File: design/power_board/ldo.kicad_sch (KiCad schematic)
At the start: 9 parts, among them U2 LM317M_DCY_4

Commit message: Add files via upload
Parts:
- removed C?: 10uF 35V, Capacitor_SMD:C_0805_2012Metric_Pad1.18x1.45mm_HandSolder, symbol Device:C
- removed C?: OPT, Capacitor_SMD:C_0805_2012Metric_Pad1.18x1.45mm_HandSolder, symbol Device:C
- added C?: 10uF, Capacitor_SMD:C_0805_2012Metric_Pad1.18x1.45mm_HandSolder, symbol Device:C
- C? (x2): value 10uF 35V -> 10uF
- R? (x2): value 442k -> _k
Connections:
- net GND: now also C?.1
- net at D?.2 (A), R?.2: now also R?.1, U2.4 (ADJUST), C?.2; no longer D?.1 (K), U2.1 (OUTPUT)
- new net: D?.1 (K), R?.1, U2.1 (OUTPUT)
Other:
- note added: "200mA output current"
- note added: "R2 = R1(VOUT/1.25 - 1)"
- note added: "Resistor values for R8 = 10k: R9 sets the voltage output for 20V R9 = 10(20/1.25 - 1) R9 = 170k for 12V: R9 = 10(12/1.25 - 1) R9 = 86k for 10V: R9 = 10(10/1.25 - 1) R9 = 70k for 5V: R9 = 10(5/1.25 - 1) R9 = 30k Both 1%"
- note removed: "A resistor between SET and GND sets the output voltage based on a 200uA current source (two LDOs). R(kΩ) = 5*VOUT"
- note removed: "The 20mR resistors somehow make the LDOs share the current, idk check the datasheet."
- note removed: "When PGFB is below 300mV fast startup is enabled. SETFS is a resistor to ground which should divide VOUT such that PGFB reaches 300mV at 90% of the desired VOUT. (pg. 21) R(kΩ) = 442 / (3*VOUT - 1)"
- moved on the sheet: R?

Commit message: Add files via upload
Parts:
- added C?: 0.1uF, Capacitor_SMD:C_0805_2012Metric_Pad1.18x1.45mm_HandSolder, symbol Device:C
- R?: value _k -> 10k
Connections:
- net GND: now also C?.2
- net VIN: now also C?.1
- net VOUT: now also U2.1 (OUTPUT); no longer D?.2 (A), U2.3 (OUTPUT)
- net at C?.2, D?.2 (A), R?.1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: now also R?.1; no longer R?.2
- new net: D?.1 (K), D?.2 (A), R?.2, U2.3 (OUTPUT)
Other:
- moved on the sheet: C?, D?, R?, U2

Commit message: Changed footprint Changed footprint path changed footprint Edit Edit Edit
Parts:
- U2: footprint footprints:DCY4 -> Package_TO_SOT_SMD:SOT-223-3_TabPin2
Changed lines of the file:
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@@
       (effects (font (size 1.524 1.524)))
     )
-    (property "Footprint" "footprints:DCY4" (at 137.16 80.01 0)
+    (property "Footprint" "Package_TO_SOT_SMD:SOT-223-3_TabPin2" (at 137.16 80.01 0)
       (effects (font (size 1.524 1.524)) hide)
     )

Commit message: Edited calculations
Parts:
- R?: value 10k -> 0.24k
- U2: value LM317M_DCY_4 -> LM317M_DCY
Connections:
- net VOUT: now also D?.1 (K), D?.2 (A), R?.2, U2.3 (OUTPUT); no longer U2.1 (OUTPUT)
- net at C?.2, D?.2 (A), R?.1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: no longer R?.1
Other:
- note added: "Resistor values for R8 = 0.24k: R9 sets the voltage output for 20V R9 = 0.24(20/1.25 - 1) R9 = 3.6k for 12V: R9 = 0.24(12/1.25 - 1) R9 = 2.06k for 10V: R9 = 0.24(10/1.25 - 1) R9 = 1.68k for 5V: R9 = 0.24(5/1.25 - 1) R9 = 0.72k Both 1%"
- note removed: "Resistor values for R8 = 10k: R9 sets the voltage output for 20V R9 = 10(20/1.25 - 1) R9 = 170k for 12V: R9 = 10(12/1.25 - 1) R9 = 86k for 10V: R9 = 10(10/1.25 - 1) R9 = 70k for 5V: R9 = 10(5/1.25 - 1) R9 = 30k Both 1%"
- moved on the sheet: C?, R?
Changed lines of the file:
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@@
 (kicad_sch (version 20230121) (generator eeschema)
   (paper "A4")
+  (junction (at 198.12 95.25) (diameter 0) (color 0 0 0 0)
+  )
   (junction (at 163.83 95.25) (diameter 0) (color 0 0 0 0)
   )
   (junction (at 201.93 78.74) (diameter 0) (color 0 0 0 0)
   )
+  (junction (at 163.83 114.3) (diameter 0) (color 0 0 0 0)
+  )
   (junction (at 179.07 114.3) (diameter 0) (color 0 0 0 0)
   )
   (junction (at 170.18 95.25) (diameter 0) (color 0 0 0 0)
   )
-  (junction (at 106.68 95.25) (diameter 0) (color 0 0 0 0)
-  )
-  (junction (at 163.83 114.3) (diameter 0) (color 0 0 0 0)
-  )
   (junction (at 189.23 78.74) (diameter 0) (color 0 0 0 0)
   )
+  (junction (at 179.07 95.25) (diameter 0) (color 0 0 0 0)
+  )
   (junction (at 170.18 78.74) (diameter 0) (color 0 0 0 0)
   )
-  (wire (pts (xy 163.83 114.3) (xy 163.83 118.11))
+  (wire (pts (xy 157.48 114.3) (xy 157.48 118.11))
     (stroke (width 0) (type default))
   )
@@
     (stroke (width 0) (type default))
   )
+  (wire (pts (xy 198.12 95.25) (xy 210.82 95.25))
+    (stroke (width 0) (type default))
+  )
   (wire (pts (xy 170.18 95.25) (xy 163.83 95.25))
     (stroke (width 0) (type default))
   )
+  (wire (pts (xy 158.75 114.3) (xy 163.83 114.3))
+    (stroke (width 0) (type default))
+  )
   (wire (pts (xy 170.18 78.74) (xy 189.23 78.74))
     (stroke (width 0) (type default))
@@
     (stroke (width 0) (type default))
   )
-  (wire (pts (xy 114.3 95.25) (xy 106.68 95.25))
-    (stroke (width 0) (type default))
-  )
   (wire (pts (xy 189.23 78.74) (xy 201.93 78.74))
     (stroke (width 0) (type default))
@@
     (stroke (width 0) (type default))
   )
-  (wire (pts (xy 106.68 95.25) (xy 90.17 95.25))
+  (wire (pts (xy 198.12 95.25) (xy 179.07 95.25))
     (stroke (width 0) (type default))
   )
@@
     (stroke (width 0) (type default))
   )
-  (wire (pts (xy 158.75 114.3) (xy 163.83 114.3))
-    (stroke (width 0) (type default))
-  )
-  (text "R2 = R1(VOUT/1.25 - 1)" (at 132.08 124.46 0)
+  (text "R2 = R1(VOUT/1.25 - 1)" (at 127 123.19 0)
     (effects (font (size 1.27 1.27)) (justify left bottom))
   )
@@
     (effects (font (size 1.27 1.27)) (justify right bottom))
   )
-  (text "Resistor values for R8 = 10k:\nR9\n sets the voltage output\nfor 20V \n	R9 = 10(20/1.25 - 1)\n	R9 = 170k\n\nfor 12V:\n  R9 = 10(12/1.25 - 1)\n  R9 = 86k\n\nfor 10V:\n  R9 = 10(10/1.25 - 1)\n  R9 = 70k\n\nfor 5V:\n  R9 = 10(5/1.25 - 1)\n  R9 = 30k\n\nBoth 1%"
-    (at 186.69 146.05 0)
+  (text "Resistor values for R8 = 0.24k:\nR9\n sets the voltage output\nfor 20V \n	R9 = 0.24(20/1.25 - 1)\n	R9 = 3.6k\n\nfor 12V:\n  R9 = 0.24(12/1.25 - 1)\n  R9 = 2.06k\n\nfor 10V:\n  R9 = 0.24(10/1.25 - 1)\n  R9 = 1.68k\n\nfor 5V:\n  R9 = 0.24(5/1.25 - 1)\n  R9 = 0.72k\n\nBoth 1%"
+    (at 242.57 134.62 0)
     (effects (font (size 1.27 1.27)) (justify left bottom))
   )
@@
     (effects (font (size 1.27 1.27)) (justify left))
   )
-  (hierarchical_label "VOUT" (shape output) (at 90.17 95.25 180) (fields_autoplaced)
-    (effects (font (size 1.27 1.27)) (justify right))
-  )
-  (symbol (lib_id "power:GND") (at 106.68 102.87 0) (mirror y) (unit 1)
-    (in_bom yes) (on_board yes) (dnp no)
-    (property "Reference" "#PWR?" (at 106.68 109.22 0)
-      (effects (font (size 1.27 1.27)) hide)
-    )
-    (property "Value" "GND" (at 106.553 107.2642 0)
-      (effects (font (size 1.27 1.27)))
-    )
-    (property "Footprint" "" (at 106.68 102.87 0)
-      (effects (font (size 1.27 1.27)) hide)
-    )
-    (property "Datasheet" "" (at 106.68 102.87 0)
+  (hierarchical_label "VOUT" (shape output) (at 210.82 95.25 0) (fields_autoplaced)
+    (effects (font (size 1.27 1.27)) (justify left))
+  )
+  (symbol (lib_id "power:GND") (at 198.12 102.87 0) (mirror y) (unit 1)
+    (in_bom yes) (on_board yes) (dnp no)
+    (property "Reference" "#PWR?" (at 198.12 109.22 0)
+      (effects (font (size 1.27 1.27)) hide)
+    )
+    (property "Value" "GND" (at 197.993 107.2642 0)
+      (effects (font (size 1.27 1.27)))
+    )
+    (property "Footprint" "" (at 198.12 102.87 0)
+      (effects (font (size 1.27 1.27)) hide)
+    )
+    (property "Datasheet" "" (at 198.12 102.87 0)
       (effects (font (size 1.27 1.27)) hide)
     )
@@
     )
   )
-  (symbol (lib_id "power:GND") (at 163.83 125.73 0) (unit 1)
-    (in_bom yes) (on_board yes) (dnp no)
-    (property "Reference" "#PWR?" (at 163.83 132.08 0)
-      (effects (font (size 1.27 1.27)) hide)
-    )
-    (property "Value" "GND" (at 163.957 130.1242 0)
-      (effects (font (size 1.27 1.27)))
-    )
-    (property "Footprint" "" (at 163.83 125.73 0)
-      (effects (font (size 1.27 1.27)) hide)
-    )
-    (property "Datasheet" "" (at 163.83 125.73 0)
+  (symbol (lib_id "power:GND") (at 157.48 125.73 0) (unit 1)
+    (in_bom yes) (on_board yes) (dnp no)
+    (property "Reference" "#PWR?" (at 157.48 132.08 0)
+      (effects (font (size 1.27 1.27)) hide)
+    )
+    (property "Value" "GND" (at 157.607 130.1242 0)
+      (effects (font (size 1.27 1.27)))
+    )
+    (property "Footprint" "" (at 157.48 125.73 0)
+      (effects (font (size 1.27 1.27)) hide)
+    )
+    (property "Datasheet" "" (at 157.48 125.73 0)
       (effects (font (size 1.27 1.27)) hide)
     )
@@
     )
   )
-  (symbol (lib_id "Device:R_US") (at 163.83 121.92 0) (unit 1)
-    (in_bom yes) (on_board yes) (dnp no)
-    (property "Reference" "R?" (at 165.5572 120.7516 0)
-      (effects (font (size 1.27 1.27)) (justify left))
-    )
-    (property "Value" "_k" (at 165.5572 123.063 0)
-      (effects (font (size 1.27 1.27)) (justify left))
-    )
-    (property "Footprint" "Resistor_SMD:R_0805_2012Metric_Pad1.20x1.40mm_HandSolder" (at 164.846 122.174 90)
-      (effects (font (size 1.27 1.27)) hide)
-    )
-    (property "Datasheet" "~" (at 163.83 121.92 0)
+  (symbol (lib_id "Device:R_US") (at 157.48 121.92 0) (unit 1)
+    (in_bom yes) (on_board yes) (dnp no)
+    (property "Reference" "R?" (at 159.2072 120.7516 0)
+      (effects (font (size 1.27 1.27)) (justify left))
+    )
+    (property "Value" "_k" (at 159.2072 123.063 0)
+      (effects (font (size 1.27 1.27)) (justify left))
+    )
+    (property "Footprint" "Resistor_SMD:R_0805_2012Metric_Pad1.20x1.40mm_HandSolder" (at 158.496 122.174 90)
+      (effects (font (size 1.27 1.27)) hide)
+    )
+    (property "Datasheet" "~" (at 157.48 121.92 0)
       (effects (font (size 1.27 1.27)) hide)
     )
@@
       (effects (font (size 1.524 1.524)))
     )
-    (property "Value" "LM317M_DCY_4" (at 137.16 76.2 0)
+    (property "Value" "LM317M_DCY" (at 137.16 76.2 0)
       (effects (font (size 1.524 1.524)))
     )
@@
     )
   )
-  (symbol (lib_id "Device:C") (at 106.68 99.06 0) (mirror y) (unit 1)
-    (in_bom yes) (on_board yes) (dnp no)
-    (property "Reference" "C?" (at 103.759 97.8916 0)
-      (effects (font (size 1.27 1.27)) (justify left))
-    )
-    (property "Value" "10uF" (at 103.759 100.203 0)
-      (effects (font (size 1.27 1.27)) (justify left))
-    )
-    (property "Footprint" "Capacitor_SMD:C_0805_2012Metric_Pad1.18x1.45mm_HandSolder" (at 105.7148 102.87 0)
-      (effects (font (size 1.27 1.27)) hide)
-    )
-    (property "Datasheet" "~" (at 106.68 99.06 0)
+  (symbol (lib_id "Device:C") (at 198.12 99.06 0) (mirror y) (unit 1)
+    (in_bom yes) (on_board yes) (dnp no)
+    (property "Reference" "C?" (at 195.199 97.8916 0)
+      (effects (font (size 1.27 1.27)) (justify left))
+    )
+    (property "Value" "10uF" (at 195.199 100.203 0)
+      (effects (font (size 1.27 1.27)) (justify left))
+    )
+    (property "Footprint" "Capacitor_SMD:C_0805_2012Metric_Pad1.18x1.45mm_HandSolder" (at 197.1548 102.87 0)
+      (effects (font (size 1.27 1.27)) hide)
+    )
+    (property "Datasheet" "~" (at 198.12 99.06 0)
       (effects (font (size 1.27 1.27)) hide)
     )
@@
       (effects (font (size 1.27 1.27)) (justify left))
     )
-    (property "Value" "10k" (at 162.56 107.95 0)
-      (effects (font (size 1.27 1.27)) (justify left))
-    )
+    (property "Value" "0.24k" (at 162.56 107.95 0)
+      (effects (font (size 1.27 1.27)) (justify left))
+    )

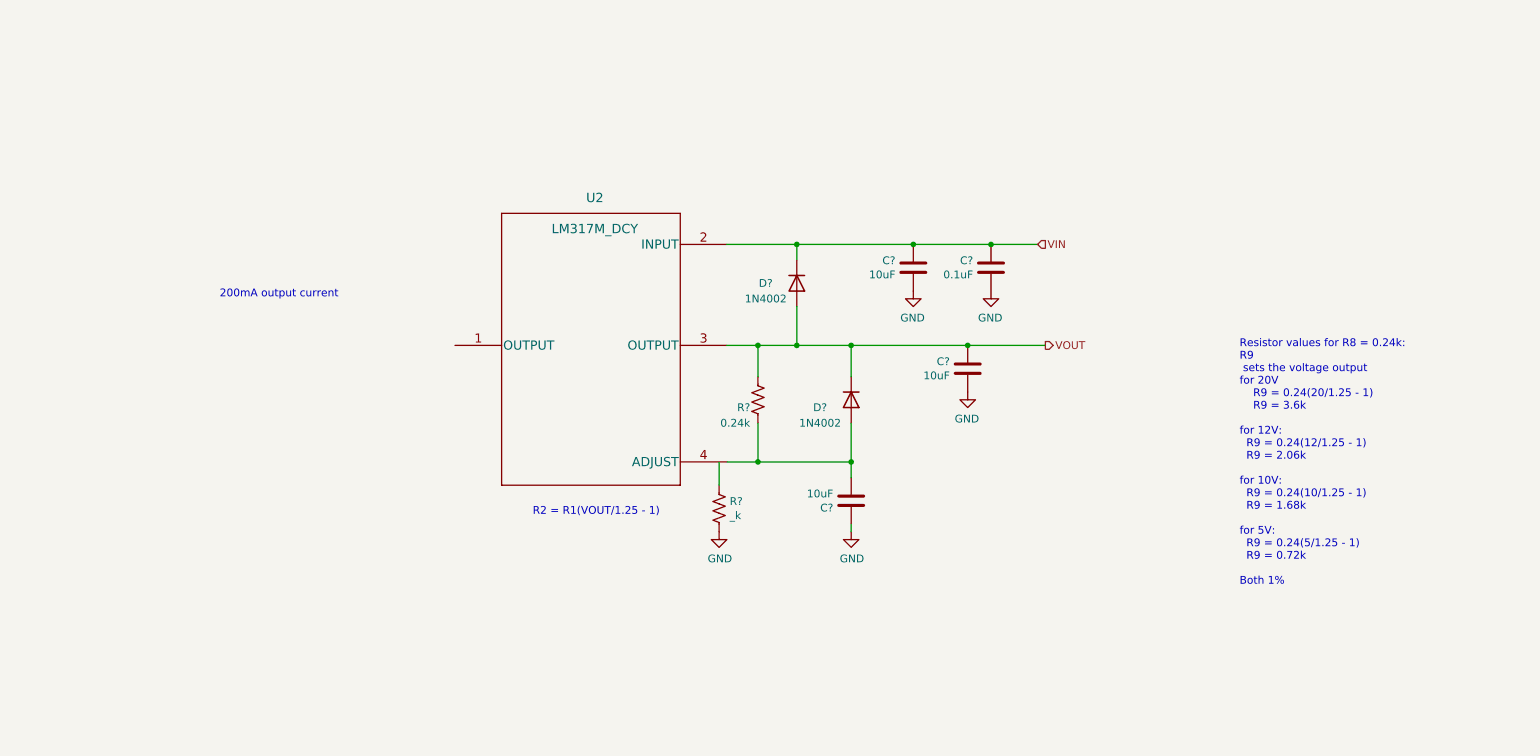
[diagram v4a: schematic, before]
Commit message: Added capacitor, switched input to right side`
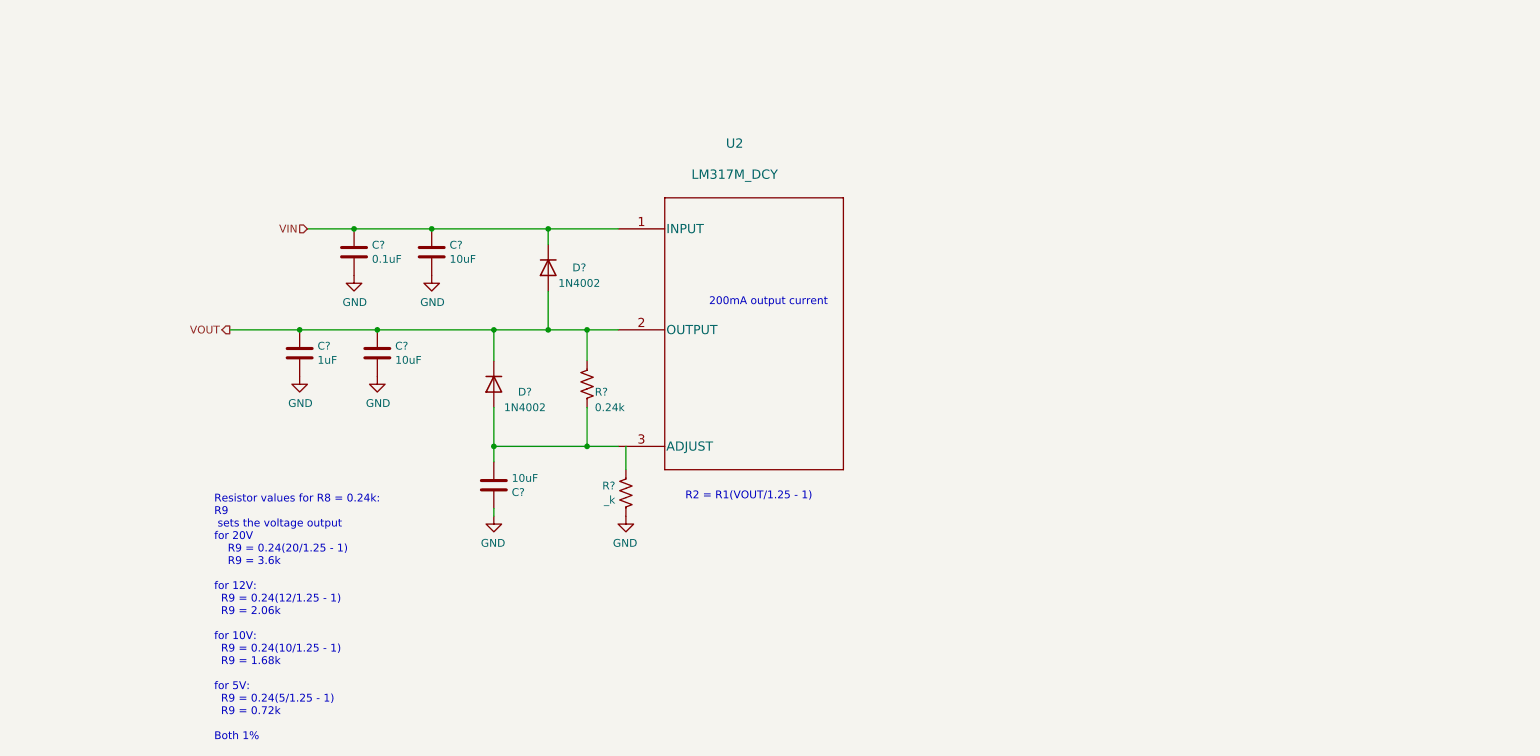
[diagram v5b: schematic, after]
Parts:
- added C?: 1uF, Capacitor_SMD:C_0805_2012Metric_Pad1.18x1.45mm_HandSolder, symbol Device:C
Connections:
- net GND: now also C?.2
- net VIN: now also U2.1 (INPUT); no longer U2.2 (INPUT)
- net VOUT: now also U2.2 (OUTPUT), C?.1; no longer U2.3 (OUTPUT)
- net at C?.2, D?.2 (A), R?.1: now also U2.3 (ADJUST); no longer U2.4 (ADJUST)
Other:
- moved on the sheet: C?, D?, R?

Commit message: i
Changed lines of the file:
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@@
   )
   (text "Resistor values for R8 = 0.24k:\nR9\n sets the voltage output\nfor 20V \n	R9 = 0.24(20/1.25 - 1)\n	R9 = 3.6k\n\nfor 12V:\n  R9 = 0.24(12/1.25 - 1)\n  R9 = 2.06k\n\nfor 10V:\n  R9 = 0.24(10/1.25 - 1)\n  R9 = 1.68k\n\nfor 5V:\n  R9 = 0.24(5/1.25 - 1)\n  R9 = 0.72k\n\nBoth 1%"
-    (at 74.93 160.02 0)
+    (at 41.91 115.57 0)
     (effects (font (size 1.27 1.27)) (justify left bottom))
   )

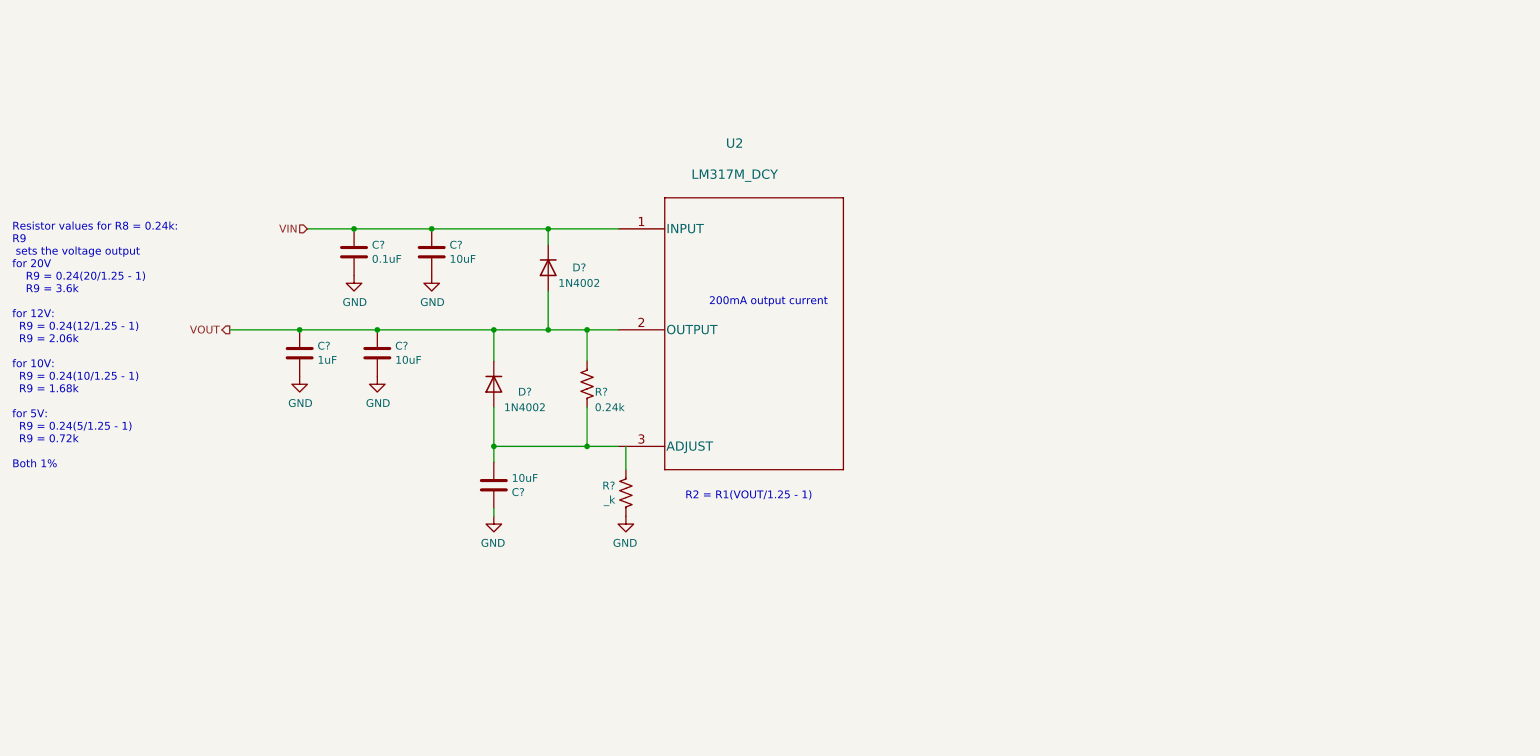
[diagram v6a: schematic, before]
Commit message: Changed layout of ldo
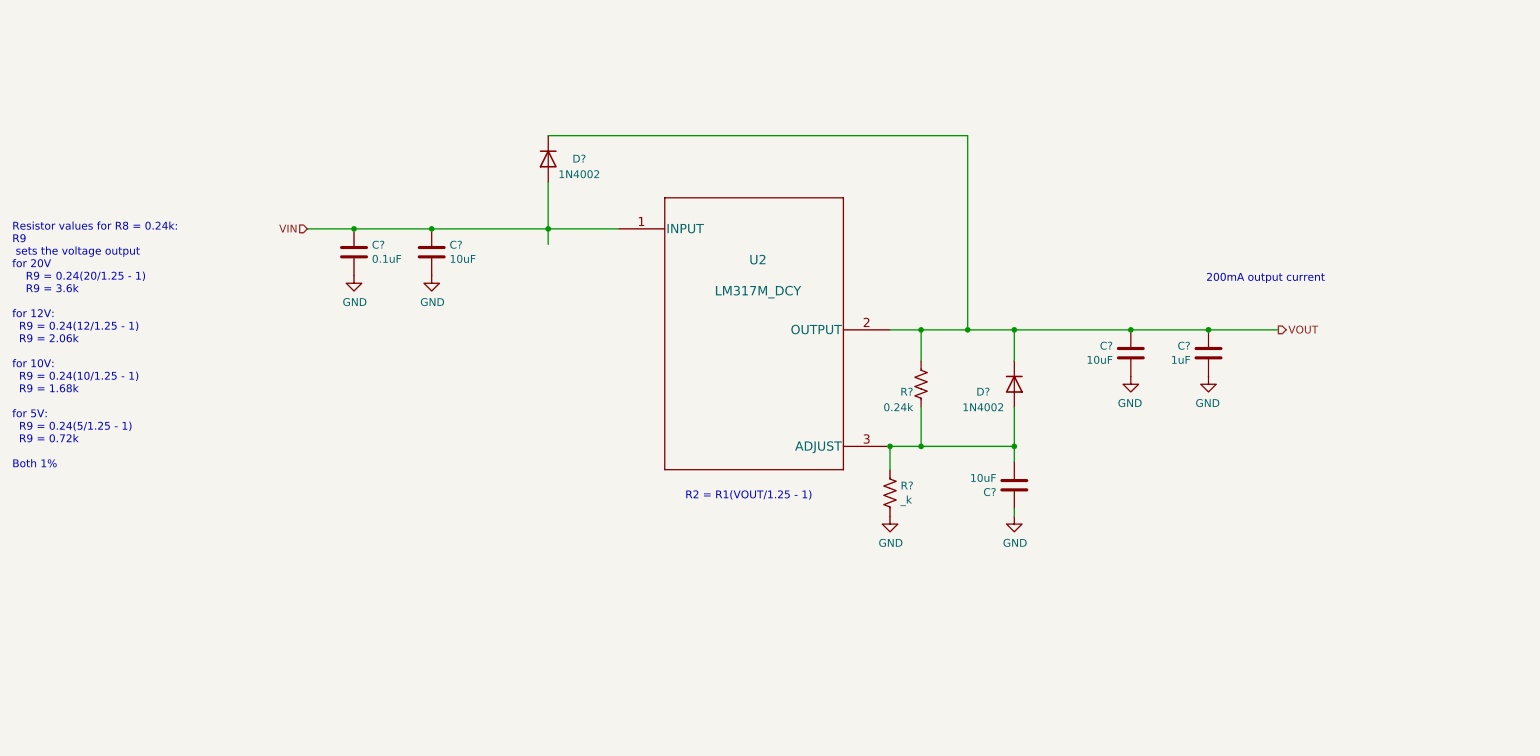
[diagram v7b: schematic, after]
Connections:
- net VIN: now also D?.2 (A); no longer D?.1 (K)
- net VOUT: now also D?.1 (K); no longer D?.2 (A)
- net at C?.2, D?.2 (A), R?.1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: now also R?.1
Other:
- moved on the sheet: C?, D?, R?, U2
